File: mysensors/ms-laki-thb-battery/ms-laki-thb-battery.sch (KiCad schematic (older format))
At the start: 2 parts, among them U1 MCP1640CH

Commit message: .
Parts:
- added C1: 4.7u, Capacitor_SMD:C_1206_3216Metric_Pad1.42x1.75mm_HandSolder, symbol Device:C_Small
- added C2: 10u, Capacitor_SMD:C_1206_3216Metric_Pad1.42x1.75mm_HandSolder, symbol Device:C_Small
- added J1: BatteryIN, Connector_PinHeader_2.54mm:PinHeader_1x02_P2.54mm_Vertical, symbol Connector:Conn_01x02_Male
- added R1: 976k0.1%, Resistor_THT:R_Axial_DIN0207_L6.3mm_D2.5mm_P7.62mm_Horizontal, symbol Device:R_Small
- added R2: 562k0.1%, Resistor_THT:R_Axial_DIN0207_L6.3mm_D2.5mm_P7.62mm_Horizontal, symbol Device:R_Small
- L1: footprint (none) -> Inductor_SMD:L_Taiyo-Yuden_NR-60xx_HandSoldering; PN (none) -> 1003.7128; Price[HUF] (none) -> 27.3; Supplier (none) -> hestore
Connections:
- net at U1.1 (SW): now also L1.2
- net Earth: now reaches U1.2 (GND)
- net Earth: now also C1.2, C2.2, J1.2 (Pin_2), R2.2
- net at U1.3 (EN): now also L1.1, U1.6 (VIN), C1.1, J1.1 (Pin_1)
- net at U1.4 (VFB): now also R1.2, R2.1
- net +3V3: now reaches U1.5 (VOUT)
- net +3V3: now also C2.1, R1.1
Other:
- moved on the sheet: L1, U1
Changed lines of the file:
@@
 EESchema Schematic File Version 4
+LIBS:ms-laki-thb-battery-cache
 EELAYER 26 0
 EELAYER END
@@
 L Regulator_Switching:MCP1640CH U1
 U 1 1 5C2F1D67
-P 2350 1500
-F 0 "U1" H 2350 1967 50  0000 C CNN
-F 1 "MCP1640CH" H 2350 1876 50  0000 C CNN
-F 2 "Package_TO_SOT_SMD:SOT-23-6" H 2400 1250 50  0001 L CIN
-F 3 "http://ww1.microchip.com/downloads/en/DeviceDoc/20002234D.pdf" H 2100 1950 50  0001 C CNN
-F 4 "hestore" H 2350 1500 50  0001 C CNN "Supplier"
-F 5 "1003.2042" H 2350 1500 50  0001 C CNN "PN"
-F 6 "227" H 2350 1500 50  0001 C CNN "Price[HUF]"
-	1    2350 1500
+P 1700 1500
+F 0 "U1" H 1700 1967 50  0000 C CNN
+F 1 "MCP1640CH" H 1700 1876 50  0000 C CNN
+F 2 "Package_TO_SOT_SMD:SOT-23-6" H 1750 1250 50  0001 L CIN
+F 3 "http://ww1.microchip.com/downloads/en/DeviceDoc/20002234D.pdf" H 1450 1950 50  0001 C CNN
+F 4 "hestore" H 1700 1500 50  0001 C CNN "Supplier"
+F 5 "1003.2042" H 1700 1500 50  0001 C CNN "PN"
+F 6 "227" H 1700 1500 50  0001 C CNN "Price[HUF]"
+	1    1700 1500
 	1    0    0    -1
 $EndComp
@@
 L pspice:INDUCTOR L1
 U 1 1 5C2F1ED2
-P 2350 900
-F 0 "L1" H 2350 1115 50  0000 C CNN
-F 1 "4.7uH" H 2350 1024 50  0000 C CNN
-F 2 "" H 2350 900 50  0001 C CNN
-F 3 "~" H 2350 900 50  0001 C CNN
-	1    2350 900
+P 1700 950
+F 0 "L1" H 1700 1165 50  0000 C CNN
+F 1 "4.7uH" H 1700 1074 50  0000 C CNN
+F 2 "Inductor_SMD:L_Taiyo-Yuden_NR-60xx_HandSoldering" H 1700 950 50  0001 C CNN
+F 3 "~" H 1700 950 50  0001 C CNN
+F 4 "hestore" H 1700 950 50  0001 C CNN "Supplier"
+F 5 "1003.7128" H 1700 950 50  0001 C CNN "PN"
+F 6 "27.3" H 1700 950 50  0001 C CNN "Price[HUF]"
+	1    1700 950
 	1    0    0    -1
 $EndComp
+$Comp
+L Device:C_Small C1
+U 1 1 5C2FBC1E
+P 1000 1400
+F 0 "C1" H 1092 1446 50  0000 L CNN
+F 1 "4.7u" H 1092 1355 50  0000 L CNN
+F 2 "Capacitor_SMD:C_1206_3216Metric_Pad1.42x1.75mm_HandSolder" H 1000 1400 50  0001 C CNN
+F 3 "https://www.hestore.hu/prod_getfile.php?id=3608" H 1000 1400 50  0001 C CNN
+F 4 "hestore" H 1000 1400 50  0001 C CNN "Supplier"
+F 5 "1000.0405" H 1000 1400 50  0001 C CNN "PN"
+F 6 "8" H 1000 1400 50  0001 C CNN "Price[HUF]"
+	1    1000 1400
+	1    0    0    -1
+$EndComp
+$Comp
+L Device:C_Small C2
+U 1 1 5C2FBCD6
+P 2700 1500
+F 0 "C2" H 2792 1546 50  0000 L CNN
+F 1 "10u" H 2792 1455 50  0000 L CNN
+F 2 "Capacitor_SMD:C_1206_3216Metric_Pad1.42x1.75mm_HandSolder" H 2700 1500 50  0001 C CNN
+F 3 "~" H 2700 1500 50  0001 C CNN
+F 4 "hestore" H 2700 1500 50  0001 C CNN "Supplier"
+F 5 "1003.1528" H 2700 1500 50  0001 C CNN "PN"
+F 6 "45.6" H 2700 1500 50  0001 C CNN "Price[HUF]"
+	1    2700 1500
+	1    0    0    -1
+$EndComp
+$Comp
+L Device:R_Small R1
+U 1 1 5C2FBDB7
+P 2200 1500
+F 0 "R1" H 2259 1546 50  0000 L CNN
+F 1 "976k0.1%" H 2259 1455 50  0000 L CNN
+F 2 "Resistor_THT:R_Axial_DIN0207_L6.3mm_D2.5mm_P7.62mm_Horizontal" H 2200 1500 50  0001 C CNN
+F 3 "https://www.hestore.hu/prod_getfile.php?id=2836" H 2200 1500 50  0001 C CNN
+F 4 "hestore" H 2200 1500 50  0001 C CNN "Supplier"
+F 5 "1002.7492" H 2200 1500 50  0001 C CNN "PN"
+F 6 "50" H 2200 1500 50  0001 C CNN "Price[HUF]"
+	1    2200 1500
+	1    0    0    -1
+$EndComp
+$Comp
+L Device:R_Small R2
+U 1 1 5C2FBE62
+P 2200 1700
+F 0 "R2" H 2259 1746 50  0000 L CNN
+F 1 "562k0.1%" H 2259 1655 50  0000 L CNN
+F 2 "Resistor_THT:R_Axial_DIN0207_L6.3mm_D2.5mm_P7.62mm_Horizontal" H 2200 1700 50  0001 C CNN
+F 3 "https://www.hestore.hu/prod_getfile.php?id=2813" H 2200 1700 50  0001 C CNN
+F 4 "hestore" H 2200 1700 50  0001 C CNN "Supplier"
+F 5 "1002.7469" H 2200 1700 50  0001 C CNN "PN"
+F 6 "51.3" H 2200 1700 50  0001 C CNN "Price[HUF]"
+	1    2200 1700
+	1    0    0    -1
+$EndComp
+Wire Wire Line
+	1450 950  1300 950
+Wire Wire Line
+	1300 950  1300 1300
+Wire Wire Line
+	1950 950  2100 950
+Wire Wire Line
+	2100 950  2100 1300
+Wire Wire Line
+	2200 1400 2100 1400
+Wire Wire Line
+	2100 1600 2200 1600
+Connection ~ 2200 1600
+Wire Wire Line
+	2200 1800 1700 1800
+Wire Wire Line
+	1300 1500 1300 1300
+Connection ~ 1300 1300
+Wire Wire Line
+	1300 1300 1000 1300
+Wire Wire Line
+	1000 1500 1000 1800
+Wire Wire Line
+	1000 1800 1700 1800
+Connection ~ 1700 1800
+Wire Wire Line
+	2700 1400 2200 1400
+Connection ~ 2200 1400
+Wire Wire Line
+	2200 1800 2700 1800
+Wire Wire Line
+	2700 1800 2700 1600
+Connection ~ 2200 1800
+$Comp
+L power:+3.3V #PWR?
+U 1 1 5C2FC53C
+P 2700 1400
+F 0 "#PWR?" H 2700 1250 50  0001 C CNN
+F 1 "+3.3V" H 2715 1573 50  0000 C CNN
+F 2 "" H 2700 1400 50  0001 C CNN
+F 3 "" H 2700 1400 50  0001 C CNN
+	1    2700 1400
+	1    0    0    -1
+$EndComp
+Connection ~ 2700 1400
+$Comp
+L power:Earth #PWR?
+U 1 1 5C2FC631
+P 1700 1800
+F 0 "#PWR?" H 1700 1550 50  0001 C CNN
+F 1 "Earth" H 1700 1650 50  0001 C CNN
+F 2 "" H 1700 1800 50  0001 C CNN
+F 3 "~" H 1700 1800 50  0001 C CNN
+	1    1700 1800
+	1    0    0    -1
+$EndComp
+$Comp
+L Connector:Conn_01x02_Male J1
+U 1 1 5C2FC689
+P 650 1300
+F 0 "J1" H 700 1400 50  0000 C CNN
+F 1 "BatteryIN" V 600 1250 50  0000 C CNN
+F 2 "Connector_PinHeader_2.54mm:PinHeader_1x02_P2.54mm_Vertical" H 650 1300 50  0001 C CNN
+F 3 "~" H 650 1300 50  0001 C CNN
+	1    650  1300
+	1    0    0    -1
+$EndComp
+Wire Wire Line
+	850  1300 1000 1300
+Connection ~ 1000 1300
+Wire Wire Line
+	850  1400 850  1800
+Wire Wire Line
+	850  1800 1000 1800
+Connection ~ 1000 1800
 $EndSCHEMATC

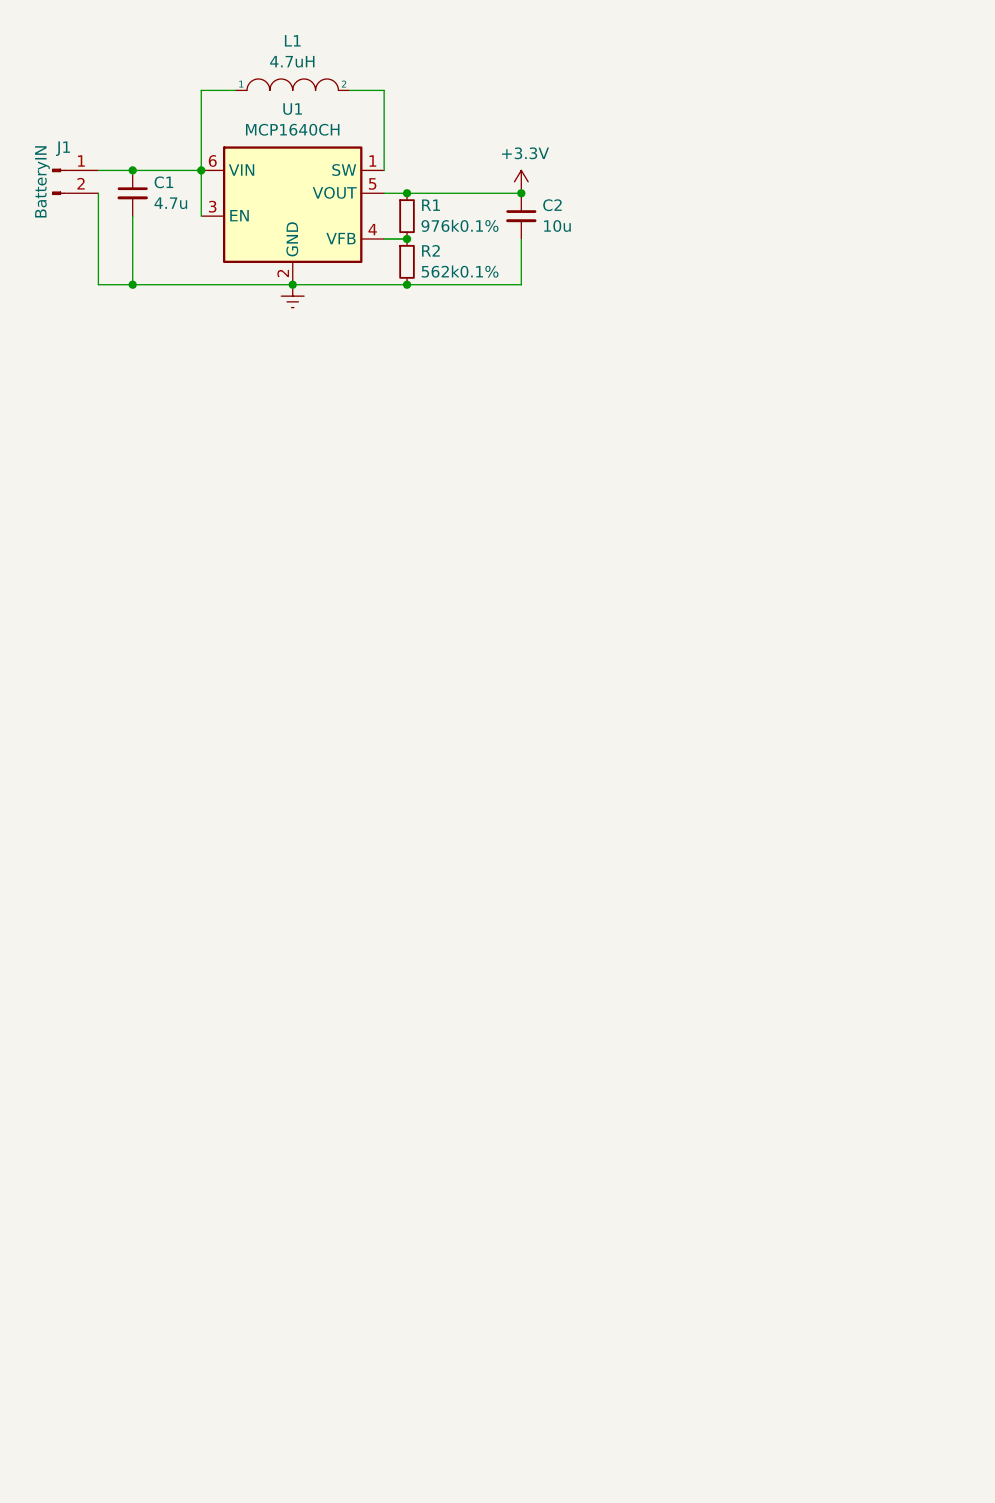
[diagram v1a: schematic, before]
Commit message: battery schemtics finsihed
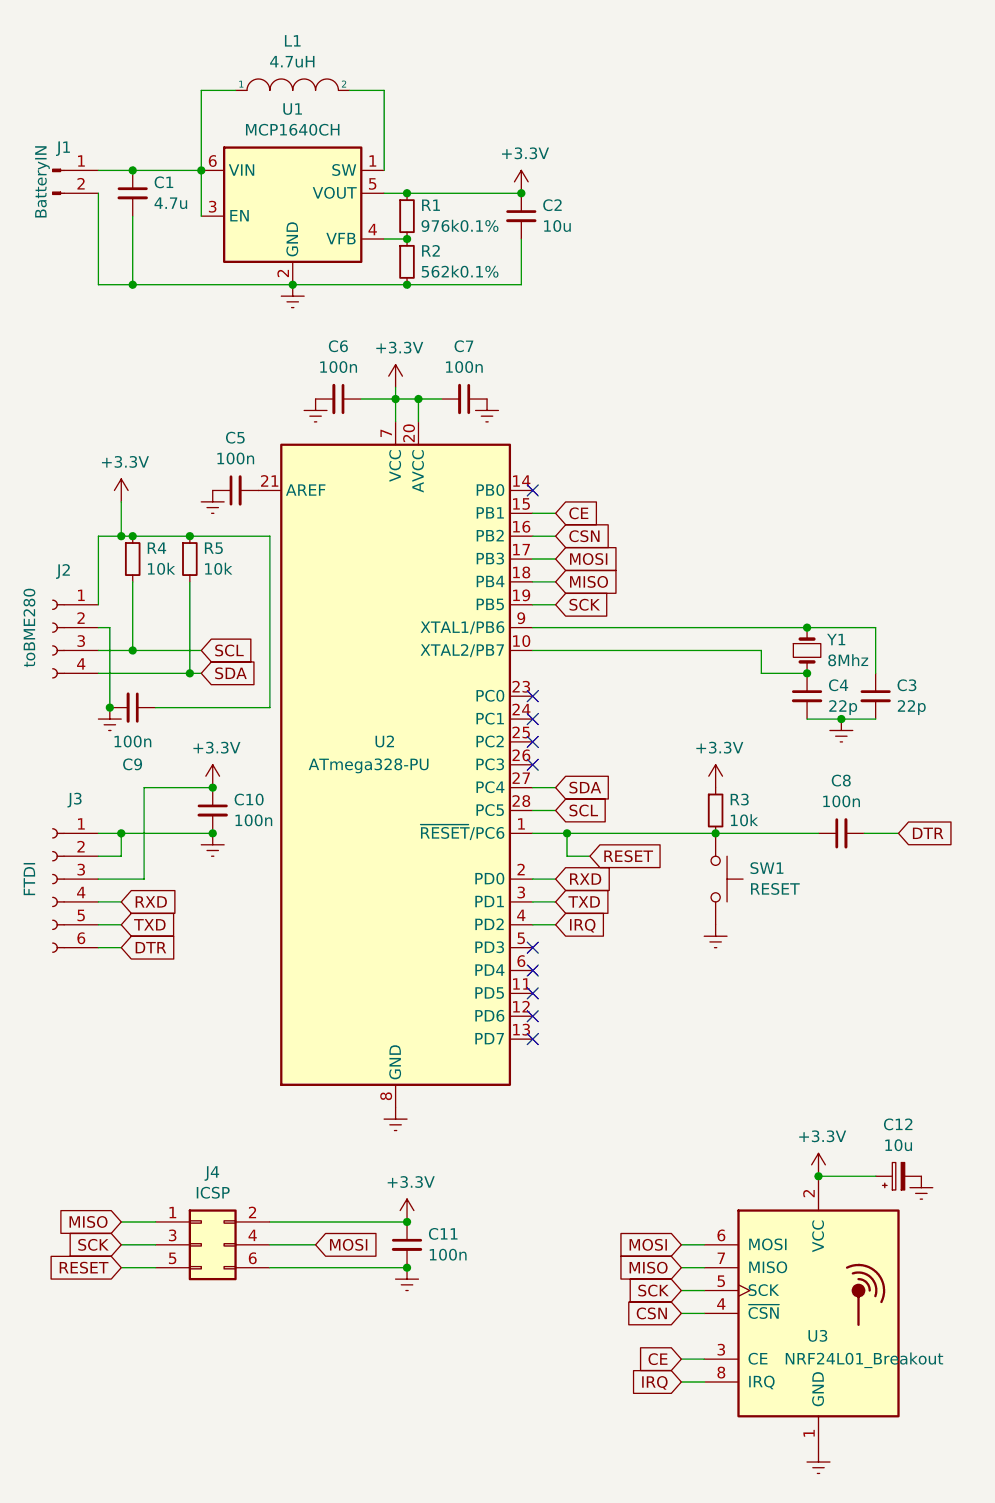
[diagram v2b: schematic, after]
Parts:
- added C10, C11, C5, C6, C7, C8, C9: 100n, Capacitor_SMD:C_1206_3216Metric_Pad1.42x1.75mm_HandSolder, symbol Device:C_Small
- added C12: 10u, symbol Device:CP_Small
- added C3, C4: 22p, Capacitor_SMD:C_1206_3216Metric_Pad1.42x1.75mm_HandSolder, symbol Device:C_Small
- added J2: toBME280, Connector_PinSocket_2.54mm:PinSocket_1x04_P2.54mm_Vertical, symbol Connector:Conn_01x04_Female
- added J3: FTDI, symbol Connector:Conn_01x06_Female
- added J4: ICSP, Connector_PinHeader_2.54mm:PinHeader_2x03_P2.54mm_Vertical, symbol Connector_Generic:Conn_02x03_Odd_Even
- added R3, R4, R5: 10k, Resistor_SMD:R_1206_3216Metric_Pad1.42x1.75mm_HandSolder, symbol Device:R_Small
- added SW1: RESET, Button_Switch_SMD:SW_SPST_FSMSM, symbol Switch:SW_Push
- added U2: ATmega328-PU, Package_DIP:DIP-28_W7.62mm_Socket_LongPads, symbol MCU_Microchip_ATmega:ATmega328-PU
- added U3: NRF24L01_Breakout, RF_Module:nRF24L01_Breakout, symbol RF:NRF24L01_Breakout
- added Y1: 8Mhz, Crystal:Crystal_HC49-U_Vertical, symbol Device:Crystal_Small
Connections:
- net +3V3: now also C10.1, C11.1, C12.1, C6.1, C7.2, C9.1, J2.1 (Pin_1), J3.3 (Pin_3), J4.2 (Pin_2), R3.1, R4.1, R5.1, U2.20 (AVCC), U2.7 (VCC), U3.2 (VCC)
- net Earth: now also C10.2, C11.2, C12.2, C3.2, C4.2, C5.1, C6.2, C7.1, C9.2, J2.2 (Pin_2), J3.1 (Pin_1), J3.2 (Pin_2), J4.6 (Pin_6), SW1.2, U2.22 (GND), U2.8 (GND), U3.1 (GND)
- new net: C4.1, U2.10 (XTAL2/PB7), Y1.2
- new net: C5.2, U2.21 (AREF)
- new net: C3.1, U2.9 (XTAL1/PB6), Y1.1
- new net CE: U2.15 (PB1), U3.3 (CE)
- new net CSN: U2.16 (PB2), U3.4 (~CSN)
- new net DTR: C8.2, J3.6 (Pin_6)
- new net IRQ: U2.4 (PD2), U3.8 (IRQ)
- new net MISO: J4.1 (Pin_1), U2.18 (PB4), U3.7 (MISO)
- new net MOSI: J4.4 (Pin_4), U2.17 (PB3), U3.6 (MOSI)
- new net RESET: C8.1, J4.5 (Pin_5), R3.2, SW1.1, U2.1 (~RESET~/PC6)
- new net RXD: J3.4 (Pin_4), U2.2 (PD0)
- new net SCK: J4.3 (Pin_3), U2.19 (PB5), U3.5 (SCK)
- new net SCL: J2.3 (Pin_3), R4.2, U2.28 (PC5)
- new net SDA: J2.4 (Pin_4), R5.2, U2.27 (PC4)
- new net TXD: J3.5 (Pin_5), U2.3 (PD1)
- no-connect marks 0 -> 10

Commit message: .
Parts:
- C12: footprint (none) -> Capacitor_THT:CP_Radial_D4.0mm_P1.50mm; PN (none) -> 1000.0404; Price[HUF] (none) -> 6.5; Supplier (none) -> hestore
- J3: footprint (none) -> Connector_PinSocket_2.54mm:PinSocket_1x06_P2.54mm_Vertical; PN (none) -> 1002.9494; Price[HUF] (none) -> 32; Supplier (none) -> hestore
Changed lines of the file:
@@
 encoding utf-8
 Sheet 1 1
-Title ""
+Title "ms-laki-thb-battery"
 Date ""
 Rev ""
@@
 Connection ~ 2200 1800
 $Comp
-L power:+3.3V #PWR?
+L power:+3.3V #PWR0101
 U 1 1 5C2FC53C
 P 2700 1400
-F 0 "#PWR?" H 2700 1250 50  0001 C CNN
+F 0 "#PWR0101" H 2700 1250 50  0001 C CNN
 F 1 "+3.3V" H 2715 1573 50  0000 C CNN
 F 2 "" H 2700 1400 50  0001 C CNN
@@
 Connection ~ 2700 1400
 $Comp
-L power:Earth #PWR?
+L power:Earth #PWR0102
 U 1 1 5C2FC631
 P 1700 1800
-F 0 "#PWR?" H 1700 1550 50  0001 C CNN
+F 0 "#PWR0102" H 1700 1550 50  0001 C CNN
 F 1 "Earth" H 1700 1650 50  0001 C CNN
 F 2 "" H 1700 1800 50  0001 C CNN
@@
 $EndComp
 $Comp
-L power:+3.3V #PWR?
+L power:+3.3V #PWR0103
 U 1 1 5C2FDB13
 P 2150 2250
-F 0 "#PWR?" H 2150 2100 50  0001 C CNN
+F 0 "#PWR0103" H 2150 2100 50  0001 C CNN
 F 1 "+3.3V" H 2165 2423 50  0000 C CNN
 F 2 "" H 2150 2250 50  0001 C CNN
@@
 	2150 2300 2150 2400
 $Comp
-L power:Earth #PWR?
+L power:Earth #PWR0104
 U 1 1 5C2FDE29
 P 2150 5400
-F 0 "#PWR?" H 2150 5150 50  0001 C CNN
+F 0 "#PWR0104" H 2150 5150 50  0001 C CNN
 F 1 "Earth" H 2150 5250 50  0001 C CNN
 F 2 "" H 2150 5400 50  0001 C CNN
@@
 	3950 3700 4100 3700
 $Comp
-L power:Earth #PWR?
+L power:Earth #PWR0105
 U 1 1 5C2FEEF1
 P 4100 3700
-F 0 "#PWR?" H 4100 3450 50  0001 C CNN
+F 0 "#PWR0105" H 4100 3450 50  0001 C CNN
 F 1 "Earth" H 4100 3550 50  0001 C CNN
 F 2 "" H 4100 3700 50  0001 C CNN
@@
 $EndComp
 $Comp
-L power:Earth #PWR?
+L power:Earth #PWR0106
 U 1 1 5C2FF14B
 P 1350 2700
-F 0 "#PWR?" H 1350 2450 50  0001 C CNN
+F 0 "#PWR0106" H 1350 2450 50  0001 C CNN
 F 1 "Earth" H 1350 2550 50  0001 C CNN
 F 2 "" H 1350 2700 50  0001 C CNN
@@
 $EndComp
 $Comp
-L power:Earth #PWR?
+L power:Earth #PWR0107
 U 1 1 5C2FF2D7
 P 1800 2300
-F 0 "#PWR?" H 1800 2050 50  0001 C CNN
+F 0 "#PWR0107" H 1800 2050 50  0001 C CNN
 F 1 "Earth" H 1800 2150 50  0001 C CNN
 F 2 "" H 1800 2300 50  0001 C CNN
@@
 $EndComp
 $Comp
-L power:Earth #PWR?
+L power:Earth #PWR0108
 U 1 1 5C2FF2FE
 P 2550 2300
-F 0 "#PWR?" H 2550 2050 50  0001 C CNN
+F 0 "#PWR0108" H 2550 2050 50  0001 C CNN
 F 1 "Earth" H 2550 2150 50  0001 C CNN
 F 2 "" H 2550 2300 50  0001 C CNN
@@
 $EndComp
 $Comp
-L power:+3.3V #PWR?
+L power:+3.3V #PWR0109
 U 1 1 5C2FFB16
 P 3550 4000
-F 0 "#PWR?" H 3550 3850 50  0001 C CNN
+F 0 "#PWR0109" H 3550 3850 50  0001 C CNN
 F 1 "+3.3V" H 3565 4173 50  0000 C CNN
 F 2 "" H 3550 4000 50  0001 C CNN
@@
 $EndComp
 $Comp
-L power:Earth #PWR?
+L power:Earth #PWR0110
 U 1 1 5C300192
 P 3550 4600
-F 0 "#PWR?" H 3550 4350 50  0001 C CNN
+F 0 "#PWR0110" H 3550 4350 50  0001 C CNN
 F 1 "Earth" H 3550 4450 50  0001 C CNN
 F 2 "" H 3550 4600 50  0001 C CNN
@@
 $EndComp
 $Comp
-L power:+3.3V #PWR?
+L power:+3.3V #PWR0111
 U 1 1 5C30372B
 P 950 2750
-F 0 "#PWR?" H 950 2600 50  0001 C CNN
+F 0 "#PWR0111" H 950 2600 50  0001 C CNN
 F 1 "+3.3V" H 965 2923 50  0000 C CNN
 F 2 "" H 950 2750 50  0001 C CNN
@@
 $EndComp
 $Comp
-L power:Earth #PWR?
+L power:Earth #PWR0112
 U 1 1 5C303979
 P 900 3650
-F 0 "#PWR?" H 900 3400 50  0001 C CNN
+F 0 "#PWR0112" H 900 3400 50  0001 C CNN
 F 1 "Earth" H 900 3500 50  0001 C CNN
 F 2 "" H 900 3650 50  0001 C CNN
@@
 F 0 "J3" H 550 4750 50  0000 C CNN
 F 1 "FTDI" V 750 4400 50  0000 C CNN
-F 2 "" H 650 4400 50  0001 C CNN
+F 2 "Connector_PinSocket_2.54mm:PinSocket_1x06_P2.54mm_Vertical" H 650 4400 50  0001 C CNN
 F 3 "~" H 650 4400 50  0001 C CNN
+F 4 "hestore" H 650 4400 50  0001 C CNN "Supplier"
+F 5 "1002.9494" H 650 4400 50  0001 C CNN "PN"
+F 6 "32" H 650 4400 50  0001 C CNN "Price[HUF]"
 	1    650  4400
 	-1   0    0    -1
 $EndComp
 $Comp
-L power:+3.3V #PWR?
+L power:+3.3V #PWR0113
 U 1 1 5C30DFDE
 P 1350 4000
-F 0 "#PWR?" H 1350 3850 50  0001 C CNN
+F 0 "#PWR0113" H 1350 3850 50  0001 C CNN
 F 1 "+3.3V" H 1365 4173 50  0000 C CNN
 F 2 "" H 1350 4000 50  0001 C CNN
@@
 $EndComp
 $Comp
-L power:Earth #PWR?
+L power:Earth #PWR0114
 U 1 1 5C30E1CD
 P 1350 4200
-F 0 "#PWR?" H 1350 3950 50  0001 C CNN
+F 0 "#PWR0114" H 1350 3950 50  0001 C CNN
 F 1 "Earth" H 1350 4050 50  0001 C CNN
 F 2 "" H 1350 4200 50  0001 C CNN
@@
 	1100 6100 950  6100
 $Comp
-L power:+3.3V #PWR?
+L power:+3.3V #PWR0115
 U 1 1 5C32A295
 P 2200 5900
-F 0 "#PWR?" H 2200 5750 50  0001 C CNN
+F 0 "#PWR0115" H 2200 5750 50  0001 C CNN
 F 1 "+3.3V" H 2215 6073 50  0000 C CNN
 F 2 "" H 2200 5900 50  0001 C CNN
@@
 Connection ~ 2200 5900
 $Comp
-L power:Earth #PWR?
+L power:Earth #PWR0116
 U 1 1 5C32A2D2
 P 2200 6100
-F 0 "#PWR?" H 2200 5850 50  0001 C CNN
+F 0 "#PWR0116" H 2200 5850 50  0001 C CNN
 F 1 "Earth" H 2200 5950 50  0001 C CNN
 F 2 "" H 2200 6100 50  0001 C CNN
@@
 $EndComp
 $Comp
-L power:+3.3V #PWR?
+L power:+3.3V #PWR0117
 U 1 1 5C32E062
 P 4000 5700
-F 0 "#PWR?" H 4000 5550 50  0001 C CNN
+F 0 "#PWR0117" H 4000 5550 50  0001 C CNN
 F 1 "+3.3V" H 4015 5873 50  0000 C CNN
 F 2 "" H 4000 5700 50  0001 C CNN
@@
 $EndComp
 $Comp
-L power:Earth #PWR?
+L power:Earth #PWR0118
 U 1 1 5C32E0A1
 P 4000 6900
-F 0 "#PWR?" H 4000 6650 50  0001 C CNN
+F 0 "#PWR0118" H 4000 6650 50  0001 C CNN
 F 1 "Earth" H 4000 6750 50  0001 C CNN
 F 2 "" H 4000 6900 50  0001 C CNN
@@
 F 0 "C12" V 4575 5700 50  0000 C CNN
 F 1 "10u" V 4484 5700 50  0000 C CNN
-F 2 "" H 4350 5700 50  0001 C CNN
+F 2 "Capacitor_THT:CP_Radial_D4.0mm_P1.50mm" H 4350 5700 50  0001 C CNN
 F 3 "~" H 4350 5700 50  0001 C CNN
+F 4 "hestore" H 4350 5700 50  0001 C CNN "Supplier"
+F 5 "1000.0404" H 4350 5700 50  0001 C CNN "PN"
+F 6 "6.5" H 4350 5700 50  0001 C CNN "Price[HUF]"
 	1    4350 5700
 	0    -1   -1   0
 $EndComp
 $Comp
-L power:Earth #PWR?
+L power:Earth #PWR0119
 U 1 1 5C32E1AF
 P 4450 5700
-F 0 "#PWR?" H 4450 5450 50  0001 C CNN
+F 0 "#PWR0119" H 4450 5450 50  0001 C CNN
 F 1 "Earth" H 4450 5550 50  0001 C CNN
 F 2 "" H 4450 5700 50  0001 C CNN
